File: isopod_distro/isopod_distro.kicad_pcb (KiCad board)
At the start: 2 copper layers, 65 x 56.5 mm, 53 parts, among them J1 CHG_IN, J10 FROM_LED, J11 FROM_LED, J12 FROM_LED, J13 FROM_LED, J14 FROM_LED, J15 FROM_LED, J16 BATT, J17 TO_LED, J18 TO_LED, J19 TO_LED, J2 TO_LED, J20 TO_LED, J21 TO_LED, J22 TO_LED, J23 FROM_LED, J24 FROM_LED, J25 FROM_LED, J26 FROM_LED, J27 FROM_LED, J28 FROM_LED, J29 BAL, J3 TO_LED, J30 Raspberry_Pi_2_3, J4 TO_LED, J5 TO_LED, J6 TO_LED, J7 TO_LED, J8 TO_DCDC, J9 FROM_DCDC, Q1 IRLR6225TRPBF, Q2 BSS138, Q3 BSS138, U1 MAX17205, U2 UPU-MAX-M8C, U3 adafruit_tdk_icm-20948

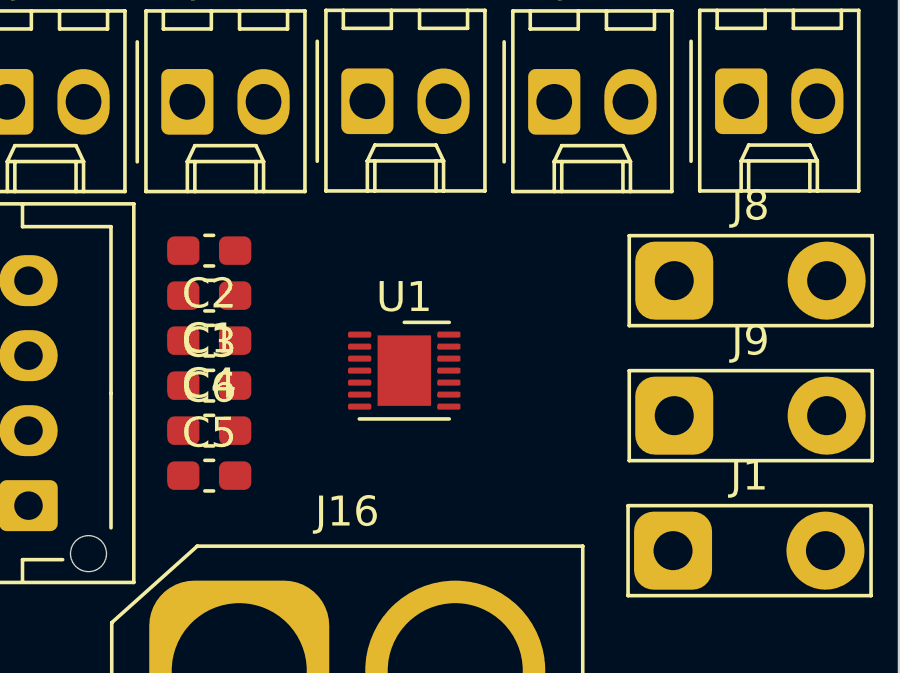
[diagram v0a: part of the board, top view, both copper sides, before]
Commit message: Assign footprints for fuel gauge resistors
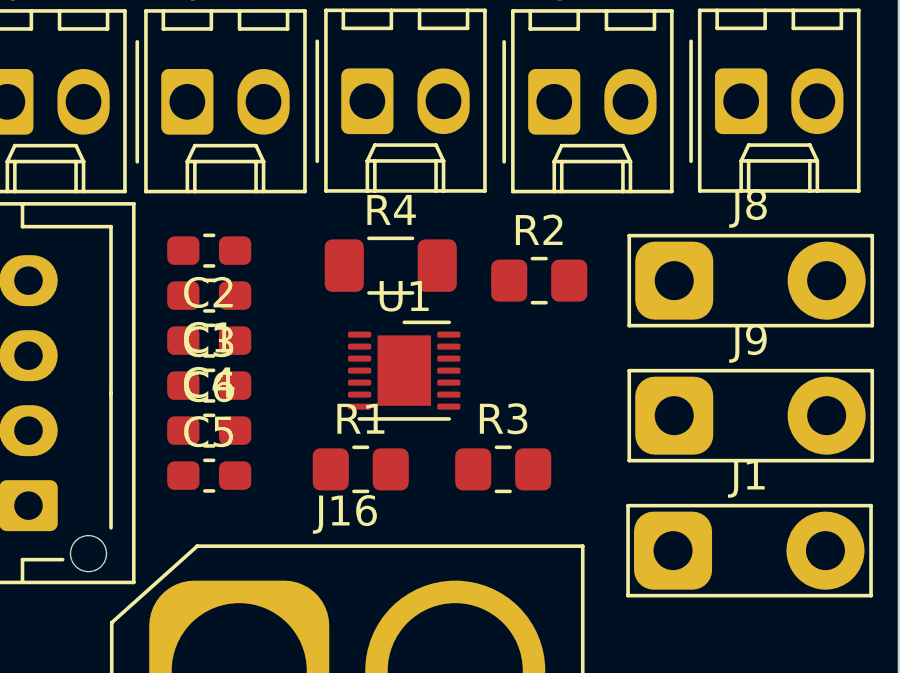
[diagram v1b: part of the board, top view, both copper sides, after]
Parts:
- added R1: 10, Resistor_SMD:R_0805_2012Metric_Pad1.20x1.40mm_HandSolder, F.Cu at (197.1, 144.8)
- added R2: 100, Resistor_SMD:R_0805_2012Metric_Pad1.20x1.40mm_HandSolder, F.Cu at (203.0, 138.5)
- added R3: 100, Resistor_SMD:R_0805_2012Metric_Pad1.20x1.40mm_HandSolder, F.Cu at (201.8, 144.8)
- added R4: 0.01R, Resistor_SMD:R_1206_3216Metric_Pad1.30x1.75mm_HandSolder, F.Cu at (198.1, 138.0)
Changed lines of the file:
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@@
+    )
+  )
+  (footprint "Resistor_SMD:R_1206_3216Metric_Pad1.30x1.75mm_HandSolder" (layer "F.Cu")
+    (at 198.05 138)
+    (descr "Resistor SMD 1206 (3216 Metric), square (rectangular) end terminal, IPC_7351 nominal with elongated pad for handsoldering. (Body size source: IPC-SM-782 page 72, https://www.pcb-3d.com/wordpress/wp-content/uploads/ipc-sm-782a_amendment_1_and_2.pdf), generated with kicad-footprint-generator")
+    (tags "resistor handsolder")
+    (property "Sheetfile" "isopod_distro.kicad_sch")
+    (property "Sheetname" "")
+    (attr smd)
+    (fp_text reference "R4" (at 0 -1.82) (layer "F.SilkS")
+      (effects (font (size 1 1) (thickness 0.15)))
+    )
+    (fp_text value "0.01R" (at 0 1.82) (layer "F.Fab")
+      (effects (font (size 1 1) (thickness 0.15)))
+    )
+    (fp_text user "${REFERENCE}" (at 0 0) (layer "F.Fab")
+      (effects (font (size 0.8 0.8) (thickness 0.12)))
+    )
+    (fp_line (start -0.727064 0.91) (end 0.727064 0.91) (layer "F.SilkS") (width 0.12))
+    (fp_line (start -0.727064 -0.91) (end 0.727064 -0.91) (layer "F.SilkS") (width 0.12))
+    (fp_line (start -2.45 1.12) (end -2.45 -1.12) (layer "F.CrtYd") (width 0.05))
+    (fp_line (start -2.45 -1.12) (end 2.45 -1.12) (layer "F.CrtYd") (width 0.05))
+    (fp_line (start 2.45 1.12) (end -2.45 1.12) (layer "F.CrtYd") (width 0.05))
+    (fp_line (start 2.45 -1.12) (end 2.45 1.12) (layer "F.CrtYd") (width 0.05))
+    (fp_line (start -1.6 0.8) (end -1.6 -0.8) (layer "F.Fab") (width 0.1))
+    (fp_line (start -1.6 -0.8) (end 1.6 -0.8) (layer "F.Fab") (width 0.1))
+    (fp_line (start 1.6 -0.8) (end 1.6 0.8) (layer "F.Fab") (width 0.1))
+    (fp_line (start 1.6 0.8) (end -1.6 0.8) (layer "F.Fab") (width 0.1))
+    (pad "1" smd roundrect (at -1.55 0) (size 1.3 1.75) (layers "F.Cu" "F.Paste" "F.Mask") (roundrect_rratio 0.192308)
+      (net 7 "Net-(C6-Pad2)") (pintype "passive"))
+    (pad "2" smd roundrect (at 1.55 0) (size 1.3 1.75) (layers "F.Cu" "F.Paste" "F.Mask") (roundrect_rratio 0.192308)
+      (net 2 "GND") (pintype "passive"))
+    (model "${KICAD6_3DMODEL_DIR}/Resistor_SMD.3dshapes/R_1206_3216Metric.wrl"
+      (offset (xyz 0 0 0))
+      (scale (xyz 1 1 1))
+      (rotate (xyz 0 0 0))
     )
   )
@@
     (pad "2" thru_hole circle (at 5.08 0) (size 2.6 2.6) (drill 1.3) (layers *.Cu *.Mask)
       (net 72 "Net-(J1-Pad2)") (pinfunction "Pin_2") (pintype "passive"))
+  )
+  (footprint "Resistor_SMD:R_0805_2012Metric_Pad1.20x1.40mm_HandSolder" (layer "F.Cu")
+    (at 197.05 144.79)
+    (descr "Resistor SMD 0805 (2012 Metric), square (rectangular) end terminal, IPC_7351 nominal with elongated pad for handsoldering. (Body size source: IPC-SM-782 page 72, https://www.pcb-3d.com/wordpress/wp-content/uploads/ipc-sm-782a_amendment_1_and_2.pdf), generated with kicad-footprint-generator")
+    (tags "resistor handsolder")
+    (property "Sheetfile" "isopod_distro.kicad_sch")
+    (property "Sheetname" "")
+    (attr smd)
+    (fp_text reference "R1" (at 0 -1.65) (layer "F.SilkS")
+      (effects (font (size 1 1) (thickness 0.15)))
+    )
+    (fp_text value "10" (at 0 1.65) (layer "F.Fab")
+      (effects (font (size 1 1) (thickness 0.15)))
+    )
+    (fp_text user "${REFERENCE}" (at 0 0) (layer "F.Fab")
+      (effects (font (size 0.5 0.5) (thickness 0.08)))
+    )
+    (fp_line (start -0.227064 -0.735) (end 0.227064 -0.735) (layer "F.SilkS") (width 0.12))
+    (fp_line (start -0.227064 0.735) (end 0.227064 0.735) (layer "F.SilkS") (width 0.12))
+    (fp_line (start 1.85 0.95) (end -1.85 0.95) (layer "F.CrtYd") (width 0.05))
+    (fp_line (start 1.85 -0.95) (end 1.85 0.95) (layer "F.CrtYd") (width 0.05))
+    (fp_line (start -1.85 -0.95) (end 1.85 -0.95) (layer "F.CrtYd") (width 0.05))
+    (fp_line (start -1.85 0.95) (end -1.85 -0.95) (layer "F.CrtYd") (width 0.05))
+    (fp_line (start 1 0.625) (end -1 0.625) (layer "F.Fab") (width 0.1))
+    (fp_line (start 1 -0.625) (end 1 0.625) (layer "F.Fab") (width 0.1))
+    (fp_line (start -1 0.625) (end -1 -0.625) (layer "F.Fab") (width 0.1))
+    (fp_line (start -1 -0.625) (end 1 -0.625) (layer "F.Fab") (width 0.1))
+    (pad "1" smd roundrect (at -1 0) (size 1.2 1.4) (layers "F.Cu" "F.Paste" "F.Mask") (roundrect_rratio 0.208333)
+      (net 72 "Net-(J1-Pad2)") (pintype "passive"))
+    (pad "2" smd roundrect (at 1 0) (size 1.2 1.4) (layers "F.Cu" "F.Paste" "F.Mask") (roundrect_rratio 0.208333)
+      (net 4 "Net-(C3-Pad1)") (pintype "passive"))
+    (model "${KICAD6_3DMODEL_DIR}/Resistor_SMD.3dshapes/R_0805_2012Metric.wrl"
+      (offset (xyz 0 0 0))
+      (scale (xyz 1 1 1))
+      (rotate (xyz 0 0 0))
+    )
   )
   (footprint "Connector_Molex:Molex_KK-254_AE-6410-03A_1x03_P2.54mm_Vertical" (layer "F.Cu")
@@
     )
   )
+  (footprint "Resistor_SMD:R_0805_2012Metric_Pad1.20x1.40mm_HandSolder" (layer "F.Cu")
+    (at 203 138.5)
+    (descr "Resistor SMD 0805 (2012 Metric), square (rectangular) end terminal, IPC_7351 nominal with elongated pad for handsoldering. (Body size source: IPC-SM-782 page 72, https://www.pcb-3d.com/wordpress/wp-content/uploads/ipc-sm-782a_amendment_1_and_2.pdf), generated with kicad-footprint-generator")
+    (tags "resistor handsolder")
+    (property "Sheetfile" "isopod_distro.kicad_sch")
+    (property "Sheetname" "")
+    (attr smd)
+    (fp_text reference "R2" (at 0 -1.65) (layer "F.SilkS")
+      (effects (font (size 1 1) (thickness 0.15)))
+    )
+    (fp_text value "100" (at 0 1.65) (layer "F.Fab")
+      (effects (font (size 1 1) (thickness 0.15)))
+    )
+    (fp_text user "${REFERENCE}" (at 0 0) (layer "F.Fab")
+      (effects (font (size 0.5 0.5) (thickness 0.08)))
+    )
+    (fp_line (start -0.227064 -0.735) (end 0.227064 -0.735) (layer "F.SilkS") (width 0.12))
+    (fp_line (start -0.227064 0.735) (end 0.227064 0.735) (layer "F.SilkS") (width 0.12))
+    (fp_line (start 1.85 0.95) (end -1.85 0.95) (layer "F.CrtYd") (width 0.05))
+    (fp_line (start -1.85 -0.95) (end 1.85 -0.95) (layer "F.CrtYd") (width 0.05))
+    (fp_line (start 1.85 -0.95) (end 1.85 0.95) (layer "F.CrtYd") (width 0.05))
+    (fp_line (start -1.85 0.95) (end -1.85 -0.95) (layer "F.CrtYd") (width 0.05))
+    (fp_line (start 1 0.625) (end -1 0.625) (layer "F.Fab") (width 0.1))
+    (fp_line (start 1 -0.625) (end 1 0.625) (layer "F.Fab") (width 0.1))
+    (fp_line (start -1 -0.625) (end 1 -0.625) (layer "F.Fab") (width 0.1))
+    (fp_line (start -1 0.625) (end -1 -0.625) (layer "F.Fab") (width 0.1))
+    (pad "1" smd roundrect (at -1 0) (size 1.2 1.4) (layers "F.Cu" "F.Paste" "F.Mask") (roundrect_rratio 0.208333)
+      (net 26 "Net-(J29-Pad3)") (pintype "passive"))
+    (pad "2" smd roundrect (at 1 0) (size 1.2 1.4) (layers "F.Cu" "F.Paste" "F.Mask") (roundrect_rratio 0.208333)
+      (net 5 "Net-(C3-Pad2)") (pintype "passive"))
+    (model "${KICAD6_3DMODEL_DIR}/Resistor_SMD.3dshapes/R_0805_2012Metric.wrl"
+      (offset (xyz 0 0 0))
+      (scale (xyz 1 1 1))
+      (rotate (xyz 0 0 0))
+    )
+  )
   (footprint "upu-max-m8c:upu-max-m8c" (layer "F.Cu")
     (at 161.5 136)
@@
     )
   )
+  (footprint "Resistor_SMD:R_0805_2012Metric_Pad1.20x1.40mm_HandSolder" (layer "F.Cu")
+    (at 201.8 144.79)
+    (descr "Resistor SMD 0805 (2012 Metric), square (rectangular) end terminal, IPC_7351 nominal with elongated pad for handsoldering. (Body size source: IPC-SM-782 page 72, https://www.pcb-3d.com/wordpress/wp-content/uploads/ipc-sm-782a_amendment_1_and_2.pdf), generated with kicad-footprint-generator")
+    (tags "resistor handsolder")
+    (property "Sheetfile" "isopod_distro.kicad_sch")
+    (property "Sheetname" "")
+    (attr smd)
+    (fp_text reference "R3" (at 0 -1.65) (layer "F.SilkS")
+      (effects (font (size 1 1) (thickness 0.15)))
+    )
+    (fp_text value "100" (at 0 1.65) (layer "F.Fab")
+      (effects (font (size 1 1) (thickness 0.15)))
+    )
+    (fp_text user "${REFERENCE}" (at 0 0) (layer "F.Fab")
+      (effects (font (size 0.5 0.5) (thickness 0.08)))
+    )
+    (fp_line (start -0.227064 -0.735) (end 0.227064 -0.735) (layer "F.SilkS") (width 0.12))
+    (fp_line (start -0.227064 0.735) (end 0.227064 0.735) (layer "F.SilkS") (width 0.12))
+    (fp_line (start 1.85 -0.95) (end 1.85 0.95) (layer "F.CrtYd") (width 0.05))
+    (fp_line (start -1.85 0.95) (end -1.85 -0.95) (layer "F.CrtYd") (width 0.05))
+    (fp_line (start -1.85 -0.95) (end 1.85 -0.95) (layer "F.CrtYd") (width 0.05))
+    (fp_line (start 1.85 0.95) (end -1.85 0.95) (layer "F.CrtYd") (width 0.05))
+    (fp_line (start -1 0.625) (end -1 -0.625) (layer "F.Fab") (width 0.1))
+    (fp_line (start -1 -0.625) (end 1 -0.625) (layer "F.Fab") (width 0.1))
+    (fp_line (start 1 0.625) (end -1 0.625) (layer "F.Fab") (width 0.1))
+    (fp_line (start 1 -0.625) (end 1 0.625) (layer "F.Fab") (width 0.1))
+    (pad "1" smd roundrect (at -1 0) (size 1.2 1.4) (layers "F.Cu" "F.Paste" "F.Mask") (roundrect_rratio 0.208333)
+      (net 25 "Net-(J29-Pad2)") (pintype "passive"))
+    (pad "2" smd roundrect (at 1 0) (size 1.2 1.4) (layers "F.Cu" "F.Paste" "F.Mask") (roundrect_rratio 0.208333)
+      (net 6 "Net-(C5-Pad2)") (pintype "passive"))
+    (model "${KICAD6_3DMODEL_DIR}/Resistor_SMD.3dshapes/R_0805_2012Metric.wrl"
+      (offset (xyz 0 0 0))
+      (scale (xyz 1 1 1))
+      (rotate (xyz 0 0 0))
+    )
+  )

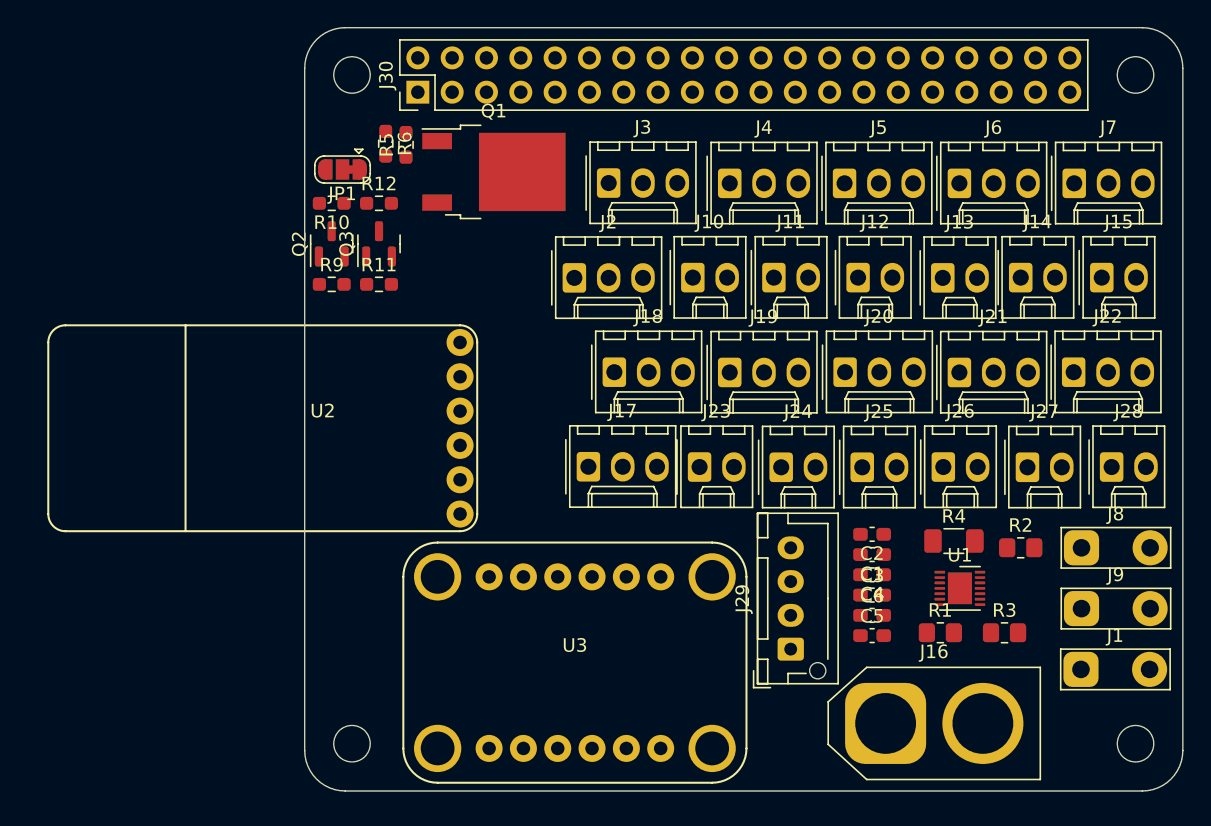
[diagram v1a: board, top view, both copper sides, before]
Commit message: Start routing PCB
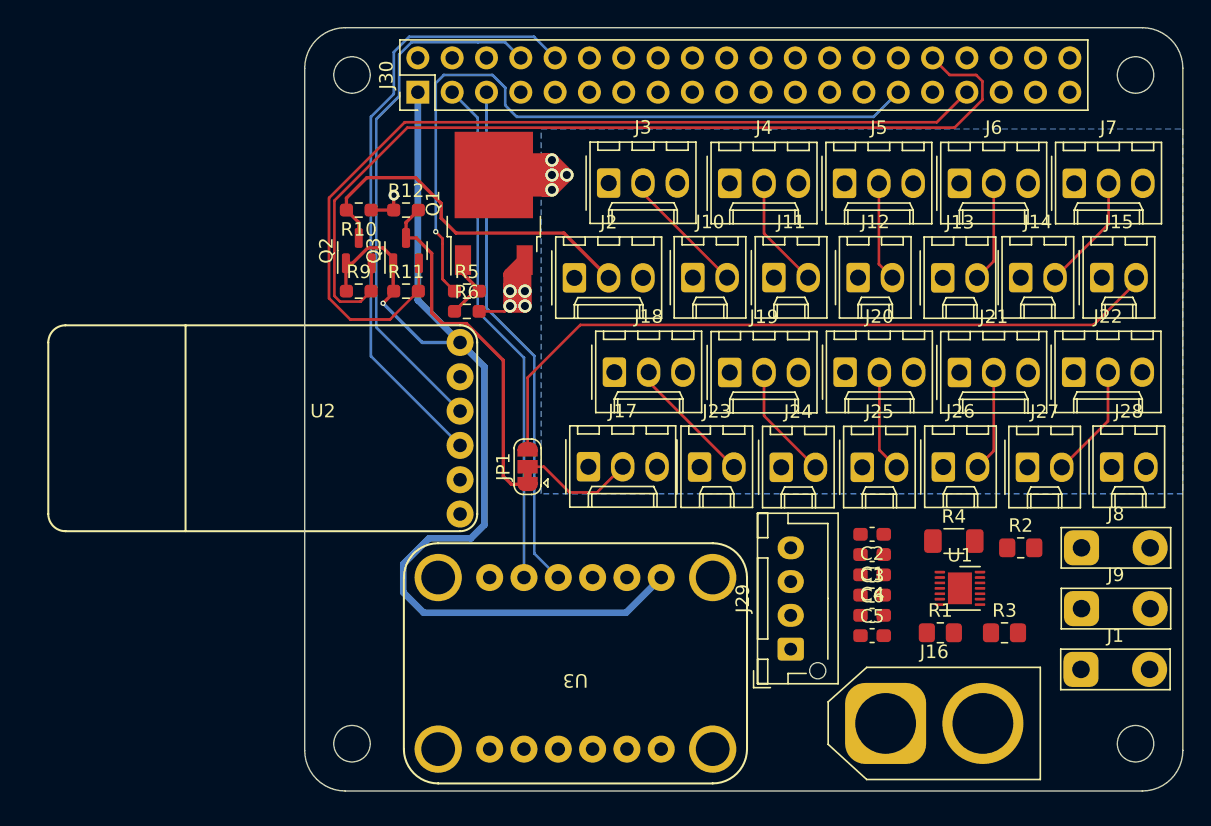
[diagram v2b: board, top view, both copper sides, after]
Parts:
- moved JP1 25.9 mm to (166.5, 132.5), turned to 90 degrees
- moved U3 24.0 mm to (180.2, 140.7), turned to 180 degrees
- moved R6 13.8 mm to (162.0, 121.0), turned to 0 degrees
- moved R5 11.7 mm to (162.0, 119.5), turned to 0 degrees
- moved Q1 2.33 mm to (164.0, 113.0), turned to 90 degrees
- moved Q2 2.06 mm to (154.0, 116.5)
- moved Q3 2.06 mm to (157.5, 116.5)
- moved R10 2.06 mm to (154.0, 113.5)
- moved R11 2.06 mm to (157.5, 119.5)
- moved R12 2.06 mm to (157.5, 113.5)
- moved R9 2.06 mm to (154.0, 119.5)
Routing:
- net +3V3: track 0.00 -> 81.1 mm, vias 0 -> 1
- net /LED_DATA_LV_1: track 0.00 -> 69.2 mm
- net /LED_DATA_LV_2: track 0.00 -> 68.1 mm
- net Net-(J15-Pad2): track 0.00 -> 53.6 mm
- net /LED_PWR_EN: track 0.00 -> 53.3 mm, vias 0 -> 1
- net /GPS_TXD: track 0.00 -> 45.6 mm
- net /GPS_RXD: track 0.00 -> 39.5 mm
- net /I2C_SCL: track 0.00 -> 38.1 mm
- net /I2C_SDA: track 0.00 -> 38.1 mm
- net /LED_DATA_1: track 0.00 -> 27.1 mm
- net /LED_DATA_2: track 0.00 -> 26.6 mm
- net /LED_GND: track 0.00 -> 24.4 mm, vias 0 -> 4
- net GND: track 0.00 -> 14.6 mm, vias 0 -> 4
- net Net-(J18-Pad2): track 0.00 -> 9.63 mm
- net Net-(J10-Pad2): track 0.00 -> 9.58 mm
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- added copper zone on In2.Cu, net +5V
- added copper zone on B.Cu, net /LED_GND
- added copper zone on In1.Cu, net GND
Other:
- copper layers 2 -> 4

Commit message: 3-pin connectors for LED return, reroute
* Use 3-pin connectors for LED return so we can supply power at both
  ends of the LED strip
* Juggle placement of the PCB again
* First draft of PCB routing
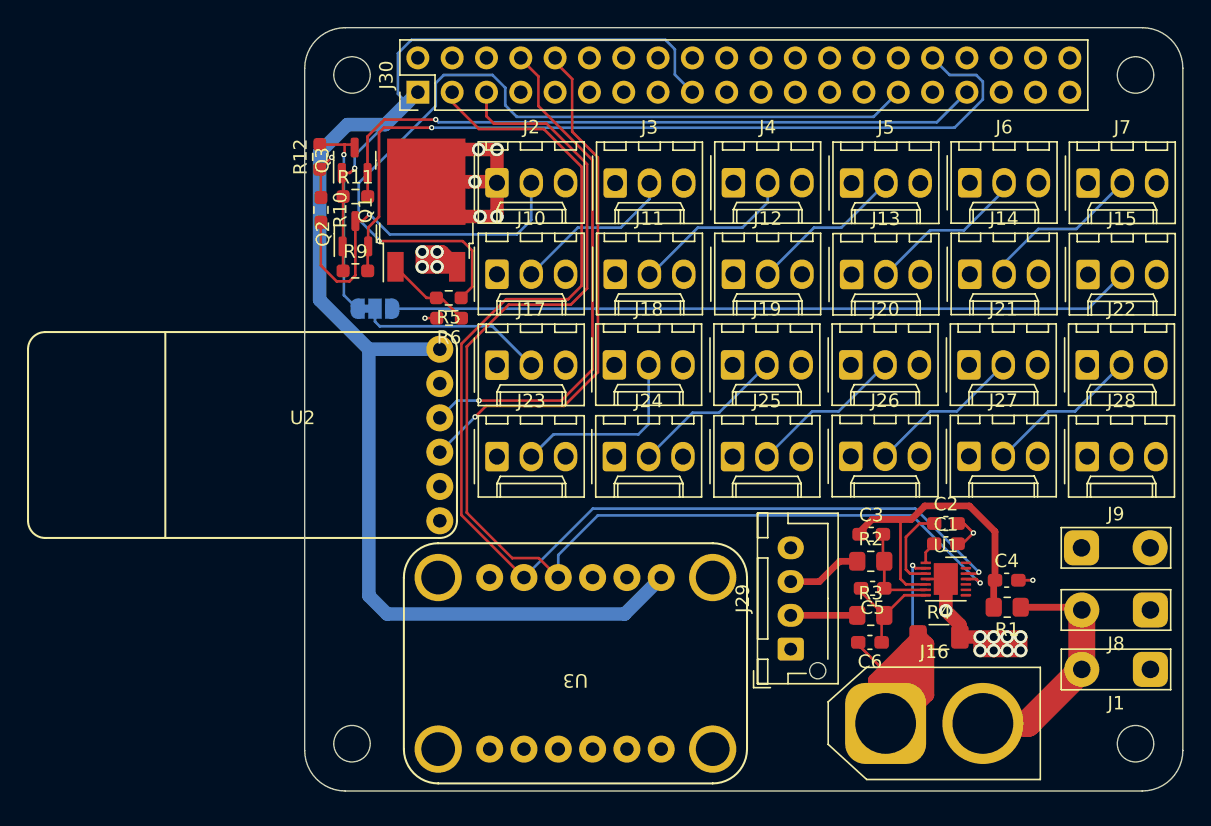
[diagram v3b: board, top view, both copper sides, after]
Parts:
- J10, J11, J12, J13, J14, J15, J23, J24, J25, J26, J27, J28: value FROM_LED -> IN; footprint Connector_Molex:Molex_KK-254_AE-6410-02A_1x02_P2.54mm_Vertical -> Connector_Molex:Molex_KK-254_AE-6410-03A_1x03_P2.54mm_Vertical
- J17, J18, J19, J2, J20, J21, J22, J3, J4, J5, J6, J7: value TO_LED -> OUT
- JP1: moved to B.Cu
- moved JP1 16.3 mm to (155.2, 120.8), turned to 0 degrees
- moved J23 15.0 mm to (164.2, 131.8)
- moved J10 14.5 mm to (164.2, 118.2)
- moved J24 12.4 mm to (172.9, 131.8)
- moved J11 11.8 mm to (173.0, 118.2)
- moved R2 11.1 mm to (191.9, 139.5)
- moved J17 10.1 mm to (164.2, 125.0)
- moved R3 9.98 mm to (191.9, 143.5)
- moved C4 9.97 mm to (202.0, 140.9), turned to 0 degrees
- moved J25 9.63 mm to (181.7, 131.8)
- moved J12 9.23 mm to (181.7, 118.2)
- moved J2 9.08 mm to (164.2, 111.5)
- moved R11 7.94 mm to (153.8, 112.5)
- moved Q3 7.69 mm to (153.7, 109.8)
- moved R12 7.50 mm to (151.1, 109.6), turned to 90 degrees
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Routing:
- net Net-(C6-Pad2): track 0.00 -> 55.4 mm, vias 0 -> 1
- net /I2C_SDA: track 38.1 -> 89.7 mm, vias 0 -> 1
- net /I2C_SCL: track 38.1 -> 89.0 mm, vias 0 -> 1
- net +3V3: track 81.1 -> 113.5 mm
- net Net-(C3-Pad1): track 0.00 -> 23.9 mm
- net Net-(J1-Pad2): track 0.00 -> 18.0 mm
- net /LED_DATA_LV_2: track 68.1 -> 50.3 mm, vias 0 -> 1
- net GND: track 14.6 -> 31.0 mm, vias 4 -> 16
- net /LED_DATA_2: track 26.6 -> 15.3 mm, vias 0 -> 1
- net /LED_PWR_EN: track 53.3 -> 63.0 mm
- net Net-(C5-Pad2): track 0.00 -> 8.48 mm
- net Net-(C3-Pad2): track 0.00 -> 7.15 mm
- net /LED_DATA_LV_1: track 69.2 -> 62.1 mm, vias 0 -> 1
- net /GPS_TXD: track 45.6 -> 38.7 mm, vias 0 -> 1
- net Net-(C2-Pad1): track 0.00 -> 6.51 mm
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- added copper zone on In1.Cu, net /LED_GND
- removed copper zone on B.Cu, net /LED_GND
